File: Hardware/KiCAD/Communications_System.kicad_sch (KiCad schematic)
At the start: 19 parts, among them IC2 CC1200RHBR, Y1 40 MHz

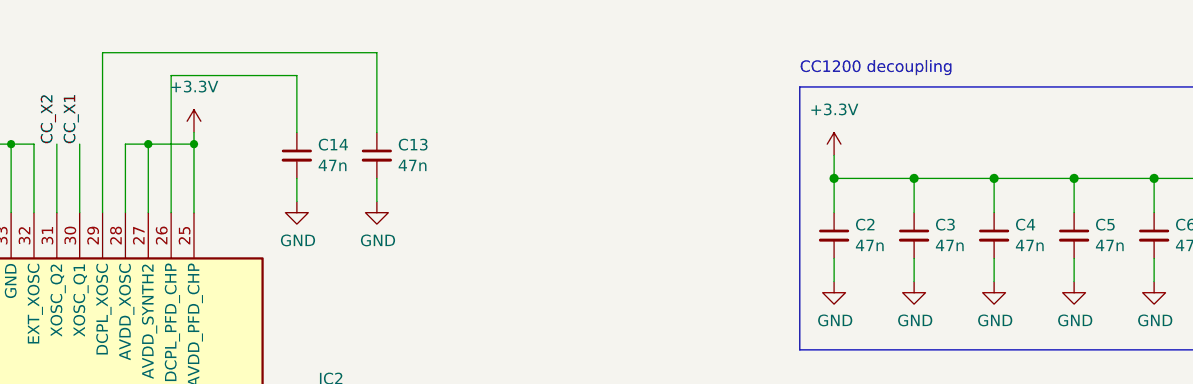
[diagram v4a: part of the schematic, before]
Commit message: Added components for amplifier, RF switch, 5v Boost, renamed footprints
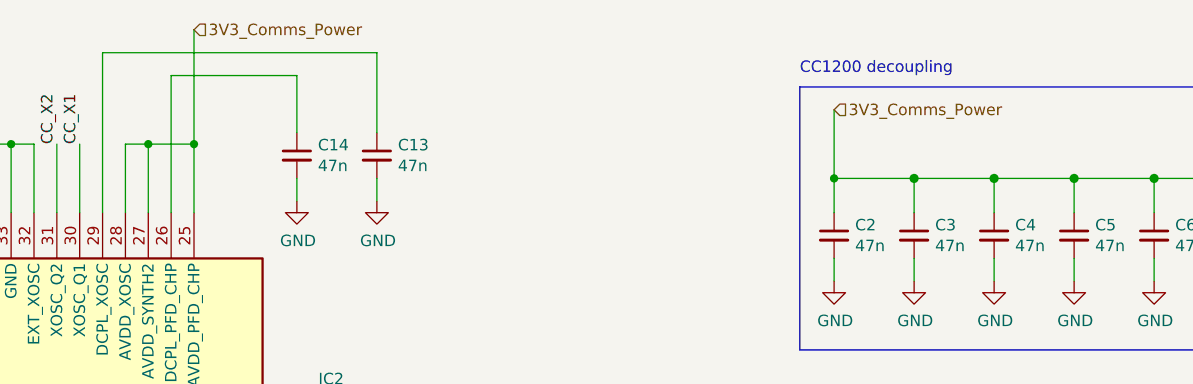
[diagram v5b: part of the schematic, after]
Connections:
- net +3.3V: no longer C10.1, C2.1, C3.1, C4.1, C5.1, C6.1, C7.1, C8.1, C9.1, IC2.25 (AVDD_PFD_CHP), IC2.27 (AVDD_SYNTH2), IC2.28 (AVDD_XOSC)
- new net 3V3_Comms_Power: C10.1, C2.1, C3.1, C4.1, C5.1, C6.1, C7.1, C8.1, C9.1, IC2.25 (AVDD_PFD_CHP), IC2.27 (AVDD_SYNTH2), IC2.28 (AVDD_XOSC)
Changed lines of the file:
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@@
     (title "RF Communications System")
   )
+  (junction (at 196.85 30.48) (diameter 0) (color 0 0 0 0)
+  )
   (junction (at 40.64 43.18) (diameter 1.016) (color 0 0 0 0)
   )
@@
   (junction (at 120.65 115.57) (diameter 0) (color 0 0 0 0)
   )
+  (junction (at 125.73 26.67) (diameter 0) (color 0 0 0 0)
+  )
   (junction (at 120.65 26.67) (diameter 0) (color 0 0 0 0)
   )
@@
   (junction (at 250.19 30.48) (diameter 0) (color 0 0 0 0)
   )
-  (junction (at 196.85 30.48) (diameter 1.016) (color 0 0 0 0)
-  )
   (junction (at 115.57 115.57) (diameter 0) (color 0 0 0 0)
   )
   (junction (at 205.74 30.48) (diameter 1.016) (color 0 0 0 0)
   )
-  (junction (at 125.73 26.67) (diameter 0) (color 0 0 0 0)
-  )
   (junction (at 22.86 127) (diameter 0) (color 0 0 0 0)
   )
@@
     (stroke (width 0) (type default))
   )
+  (wire (pts (xy 125.73 13.97) (xy 125.73 26.67))
+    (stroke (width 0) (type default))
+  )
   (wire (pts (xy 125.73 34.29) (xy 125.73 26.67))
     (stroke (width 0) (type default))
@@
     (stroke (width 0) (type solid))
   )
-  (wire (pts (xy 196.85 27.94) (xy 196.85 30.48))
-    (stroke (width 0) (type solid))
-  )
   (wire (pts (xy 137.16 19.05) (xy 137.16 25.4))
     (stroke (width 0) (type default))
@@
     (stroke (width 0) (type default))
   )
+  (wire (pts (xy 196.85 22.86) (xy 196.85 30.48))
+    (stroke (width 0) (type default))
+  )
   (wire (pts (xy 232.41 39.37) (xy 232.41 41.91))
     (stroke (width 0) (type solid))
@@
   )
   (wire (pts (xy 120.65 34.29) (xy 120.65 26.67))
-    (stroke (width 0) (type default))
-  )
-  (wire (pts (xy 125.73 25.4) (xy 125.73 26.67))
     (stroke (width 0) (type default))
   )
@@
     (effects (font (size 1.27 1.27)) (justify right))
   )
+  (hierarchical_label "3V3_Comms_Power" (shape input) (at 125.73 13.97 0) (fields_autoplaced)
+    (effects (font (size 1.27 1.27)) (justify left))
+  )
   (hierarchical_label "CC_GPIO0" (shape bidirectional) (at 107.95 107.95 270) (fields_autoplaced)
     (effects (font (size 1.27 1.27)) (justify right))
@@
   (hierarchical_label "CC_MISO" (shape output) (at 105.41 107.95 270) (fields_autoplaced)
     (effects (font (size 1.27 1.27)) (justify right))
+  )
+  (hierarchical_label "3V3_Comms_Power" (shape input) (at 196.85 22.86 0) (fields_autoplaced)
+    (effects (font (size 1.27 1.27)) (justify left))
   )
   (hierarchical_label "LNA_P" (shape input) (at 146.05 72.39 0) (fields_autoplaced)
@@
     )
   )
-  (symbol (lib_id "power:+3.3V") (at 125.73 25.4 0) (unit 1)
-    (in_bom yes) (on_board yes) (dnp no) (fields_autoplaced)
-    (property "Reference" "#PWR025" (at 125.73 29.21 0)
-      (effects (font (size 1.27 1.27)) hide)
-    )
-    (property "Value" "+3.3V" (at 125.73 20.32 0)
-      (effects (font (size 1.27 1.27)))
-    )
-    (property "Footprint" "" (at 125.73 25.4 0)
-      (effects (font (size 1.27 1.27)) hide)
-    )
-    (property "Datasheet" "" (at 125.73 25.4 0)
-      (effects (font (size 1.27 1.27)) hide)
-    )
-    (pin "1")
-    (instances
-      (project "Cobalt-Cowboy"
-        (path "/60a68eb1-aa0f-414e-b03b-965ad6b52dab/1039084b-a0e1-47ac-823b-a237cfc3ed39"
-          (reference "#PWR025") (unit 1)
-        )
-        (path "/60a68eb1-aa0f-414e-b03b-965ad6b52dab/d80d452c-0cd9-4253-b692-c2cdb4b1394b"
-          (reference "#PWR03") (unit 1)
-        )
-      )
-    )
-  )
   (symbol (lib_id "power:GND") (at 22.86 132.08 0) (unit 1)
     (in_bom yes) (on_board yes) (dnp no)
@@
         )
       )
-    )
-  )
-  (symbol (lib_id "power:+3.3V") (at 196.85 27.94 0) (unit 1)
-    (in_bom yes) (on_board yes) (dnp no) (fields_autoplaced)
-    (property "Reference" "#PWR025" (at 196.85 31.75 0)
-      (effects (font (size 1.27 1.27)) hide)
-    )
-    (property "Value" "+3.3V" (at 196.85 22.86 0)
-      (effects (font (size 1.27 1.27)))
-    )
-    (property "Footprint" "" (at 196.85 27.94 0)
-      (effects (font (size 1.27 1.27)) hide)
-    )
-    (property "Datasheet" "" (at 196.85 27.94 0)
-      (effects (font (size 1.27 1.27)) hide)
-    )
-    (pin "1")
-    (instances
-      (project "Cobalt-Cowboy"
-        (path "/60a68eb1-aa0f-414e-b03b-965ad6b52dab/1039084b-a0e1-47ac-823b-a237cfc3ed39"
-          (reference "#PWR025") (unit 1)
-        )
-        (path "/60a68eb1-aa0f-414e-b03b-965ad6b52dab/d80d452c-0cd9-4253-b692-c2cdb4b1394b"
-          (reference "#PWR034") (unit 1)
-        )
-      )

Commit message: feat: corrected Power routing, added TODOs for board, prepared for amps
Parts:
- added IC4: BQ24193RGER, Cobalt_Cowboy:QFN50P400X400X100-25N-D_BQ24193RGER, symbol Cobalt-Cowboy:BQ24193RGER
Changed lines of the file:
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@@
+    )
+  )
+  (symbol (lib_id "Cobalt-Cowboy:BQ24193RGER") (at 199.39 97.79 0) (unit 1)
+    (in_bom yes) (on_board yes) (dnp no) (fields_autoplaced)
+    (property "Reference" "IC4" (at 238.76 90.8619 0)
+      (effects (font (size 1.27 1.27)))
+    )
+    (property "Value" "BQ24193RGER" (at 238.76 93.4019 0)
+      (effects (font (size 1.27 1.27)))
+    )
+    (property "Footprint" "Cobalt_Cowboy:QFN50P400X400X100-25N-D_BQ24193RGER" (at 231.14 182.55 0)
+      (effects (font (size 1.27 1.27)) (justify left top) hide)
+    )
+    (property "Datasheet" "http://www.ti.com/lit/gpn/bq24193" (at 231.14 282.55 0)
+      (effects (font (size 1.27 1.27)) (justify left top) hide)
+    )
+    (property "Height" "1" (at 231.14 482.55 0)
+      (effects (font (size 1.27 1.27)) (justify left top) hide)
+    )
+    (property "Manufacturer_Name" "Texas Instruments" (at 231.14 582.55 0)
+      (effects (font (size 1.27 1.27)) (justify left top) hide)
+    )
+    (property "Manufacturer_Part_Number" "BQ24193RGER" (at 231.14 682.55 0)
+      (effects (font (size 1.27 1.27)) (justify left top) hide)
+    )
+    (property "Mouser Part Number" "595-BQ24193RGER" (at 231.14 782.55 0)
+      (effects (font (size 1.27 1.27)) (justify left top) hide)
+    )
+    (property "Mouser Price/Stock" "https://www.mouser.co.uk/ProductDetail/Texas-Instruments/BQ24193RGER?qs=E2%2FxqS9xjzprfPaRl%2FdVSQ%3D%3D" (at 231.14 882.55 0)
+      (effects (font (size 1.27 1.27)) (justify left top) hide)
+    )
+    (property "Arrow Part Number" "BQ24193RGER" (at 231.14 982.55 0)
+      (effects (font (size 1.27 1.27)) (justify left top) hide)
+    )
+    (property "Arrow Price/Stock" "https://www.arrow.com/en/products/bq24193rger/texas-instruments" (at 231.14 1082.55 0)
+      (effects (font (size 1.27 1.27)) (justify left top) hide)
+    )
+    (pin "19")
+    (pin "16")
+    (pin "10")
+    (pin "6")
+    (pin "2")
+    (pin "25")
+    (pin "15")
+    (pin "1")
+    (pin "4")
+    (pin "21")
+    (pin "8")
+    (pin "5")
+    (pin "18")
+    (pin "11")
+    (pin "20")
+    (pin "3")
+    (pin "14")
+    (pin "13")
+    (pin "23")
+    (pin "22")
+    (pin "7")
+    (pin "17")
+    (pin "9")
+    (pin "12")
+    (pin "24")
+    (instances
+      (project "Cobalt-Cowboy"
+        (path "/60a68eb1-aa0f-414e-b03b-965ad6b52dab/2f7042f8-0d23-4099-8d81-3056d19c4a6f"
+          (reference "IC4") (unit 1)
+        )
+        (path "/60a68eb1-aa0f-414e-b03b-965ad6b52dab/d80d452c-0cd9-4253-b692-c2cdb4b1394b"
+          (reference "IC6") (unit 1)
+        )
+      )
     )
   )

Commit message: Changed Keypad to better accomidate use of GPIO and removed inc symbols
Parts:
- removed IC4: BQ24193RGER, Cobalt_Cowboy:QFN50P400X400X100-25N-D_BQ24193RGER, symbol Cobalt-Cowboy:BQ24193RGER
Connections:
- net +3.3V: no longer IC2.2 (RESET_N)
- net GND: no longer IC2.7 (SI), IC2.8 (SCLK), IC2.9 (SO_(GPIO1))
- new net CC_MISO: IC2.9 (SO_(GPIO1))
- new net CC_MOSI: IC2.7 (SI)
- new net CC_NRST: IC2.2 (RESET_N)
- new net CC_SCLK: IC2.8 (SCLK)
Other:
- note added: "CC1200 XTAL: No external clock. TODO: Replace with a TCXO"
- note removed: "CC1200 Reset: Always active."
- note removed: "CC1200 Serial: In Non-Legacy Mode."
- note removed: "CC1200 XTAL: No external clock."

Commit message: Added 3.3v converter
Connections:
- net +3.3V: no longer IC2.12 (DVDD_2), IC2.13 (AVDD_IF), IC2.15 (AVDD_RF)
- net 3V3_Comms_Power: now also IC2.12 (DVDD_2), IC2.13 (AVDD_IF), IC2.15 (AVDD_RF)
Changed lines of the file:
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@@
     (effects (font (size 1.27 1.27)) (justify right))
+  )
+  (hierarchical_label "3V3_Comms_Power" (shape input) (at 137.16 102.87 0) (fields_autoplaced)
+    (effects (font (size 1.27 1.27)) (justify left))
   )
   (hierarchical_label "PA" (shape input) (at 146.05 77.47 0) (fields_autoplaced)
@@
         )
       )
-    )
-  )
-  (symbol (lib_id "power:+3.3V") (at 137.16 102.87 0) (unit 1)
-    (in_bom yes) (on_board yes) (dnp no) (fields_autoplaced)
-    (property "Reference" "#PWR025" (at 137.16 106.68 0)
-      (effects (font (size 1.27 1.27)) hide)
-    )
-    (property "Value" "+3.3V" (at 137.16 97.79 0)
-      (effects (font (size 1.27 1.27)))
-    )
-    (property "Footprint" "" (at 137.16 102.87 0)
-      (effects (font (size 1.27 1.27)) hide)
-    )
-    (property "Datasheet" "" (at 137.16 102.87 0)
-      (effects (font (size 1.27 1.27)) hide)
-    )
-    (pin "1")
-    (instances
-      (project "Cobalt-Cowboy"
-        (path "/60a68eb1-aa0f-414e-b03b-965ad6b52dab/1039084b-a0e1-47ac-823b-a237cfc3ed39"
-          (reference "#PWR025") (unit 1)
-        )
-        (path "/60a68eb1-aa0f-414e-b03b-965ad6b52dab/d80d452c-0cd9-4253-b692-c2cdb4b1394b"
-          (reference "#PWR022") (unit 1)
-        )
-      )
